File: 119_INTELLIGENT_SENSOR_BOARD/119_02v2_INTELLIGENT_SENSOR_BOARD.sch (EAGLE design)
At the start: 14 parts

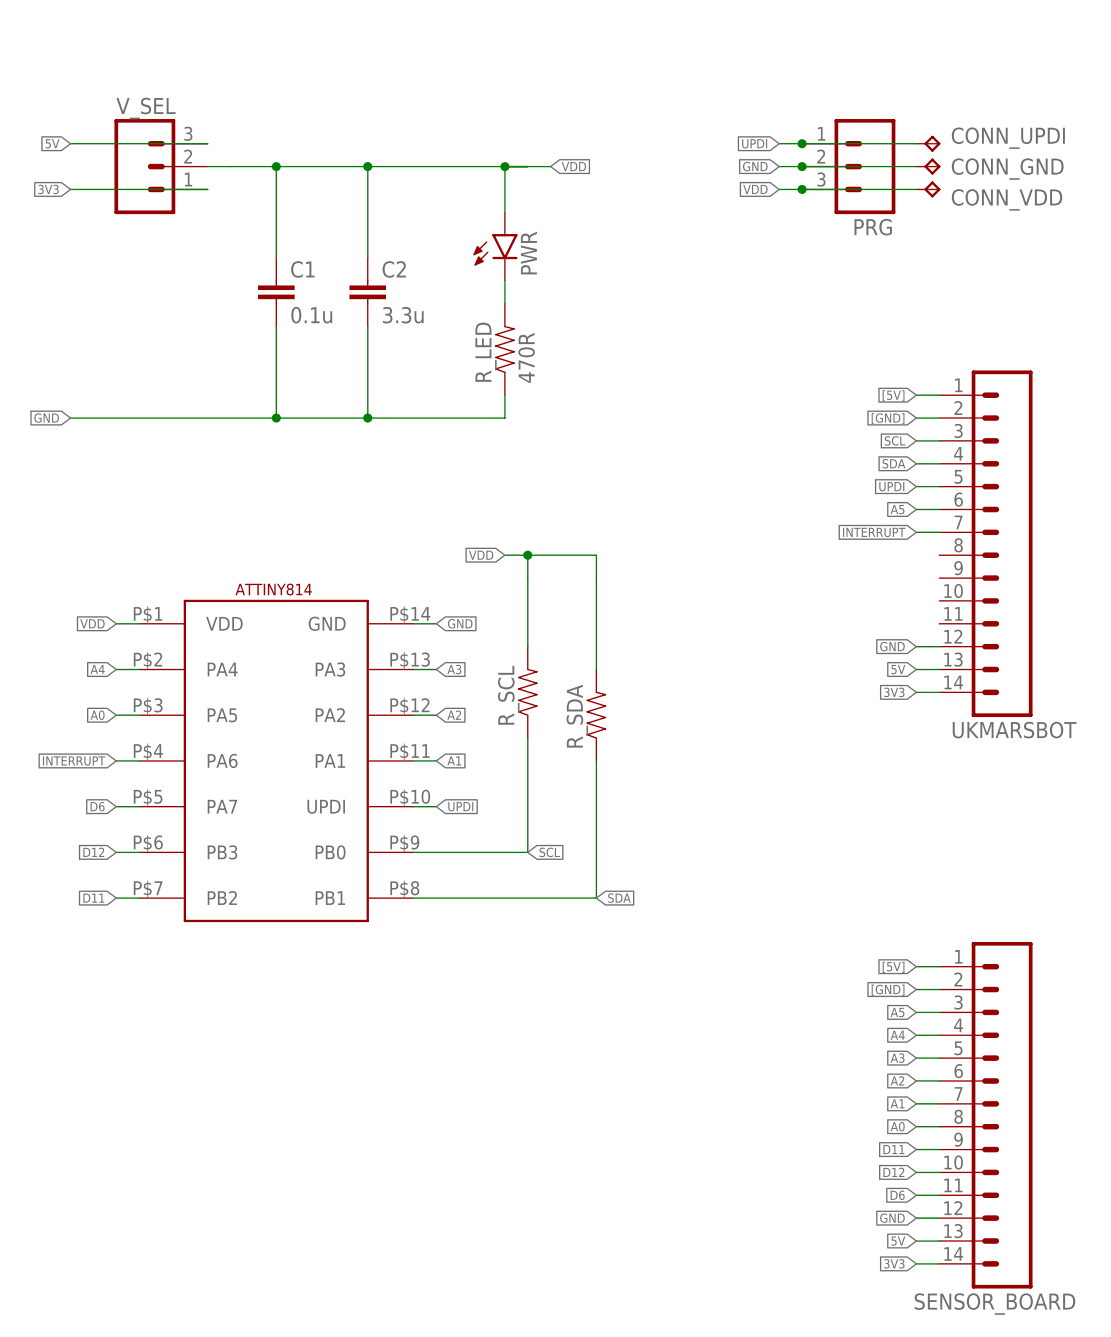
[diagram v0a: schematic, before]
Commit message: Formed new documentation
Split manual into datasheet, library and notes... added a few more ISC library header defines
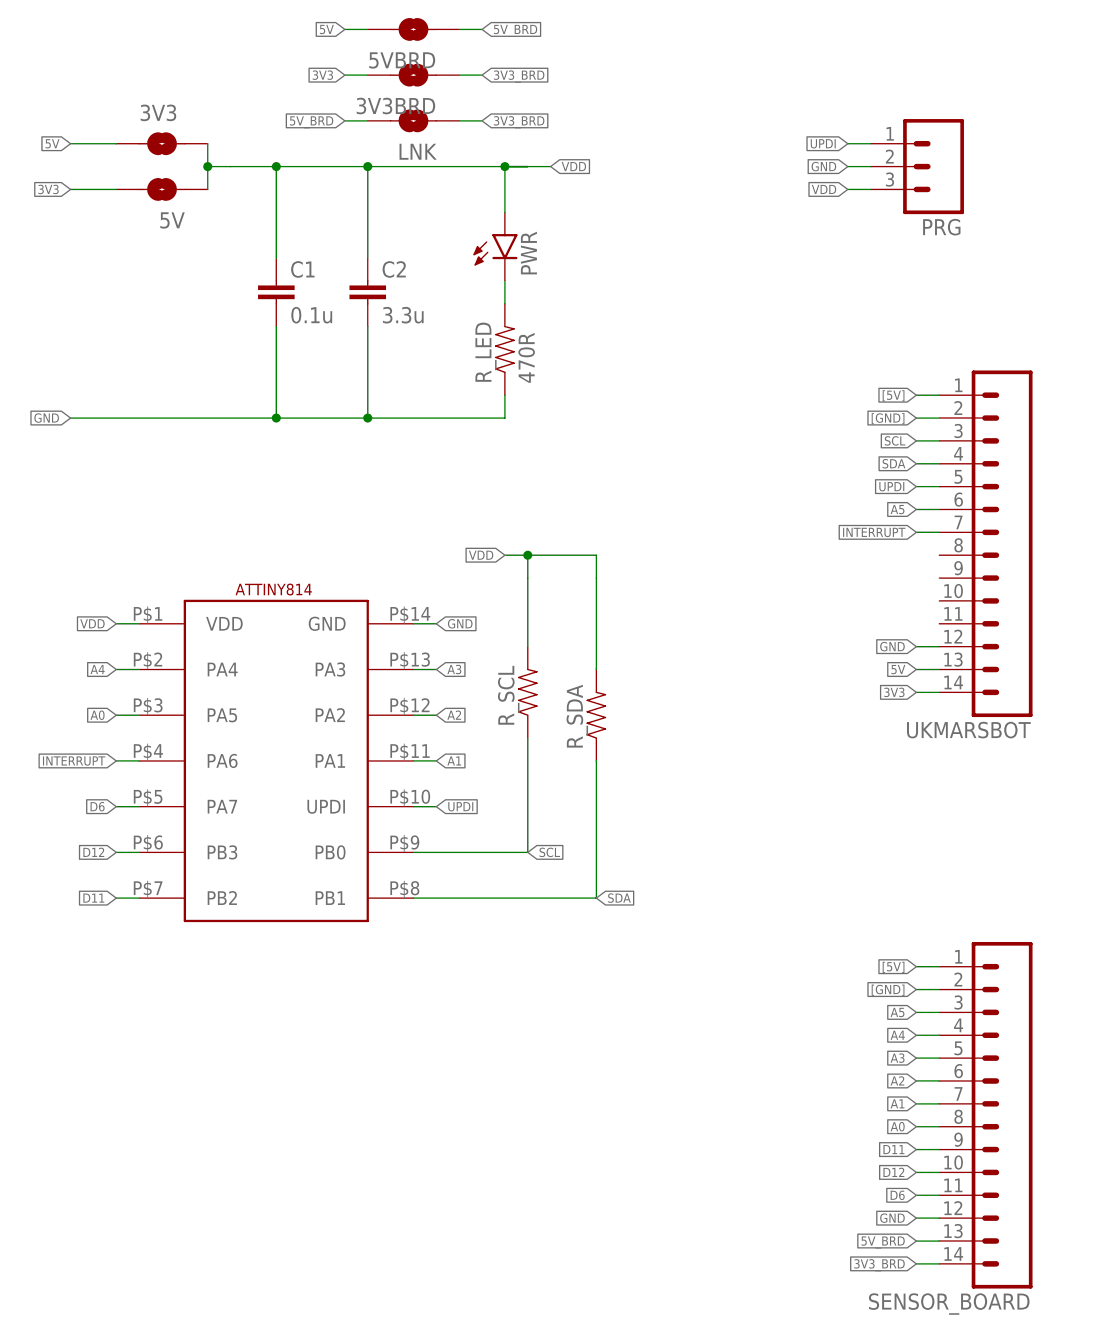
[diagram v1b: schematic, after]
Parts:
- removed CONN_GND, CONN_UPDI, CONN_VDD: TPB1,27, testpad:TPB1,27
- removed V_SEL: (no value), SparkFun-Connectors:M03PTH
- added 3V3, 3V3BRD, 5V, 5VBRD, LNK: JUMPER-SMT_2_NO_SILK, SparkFun-Jumpers:JUMPER-SMT_2_NO_SILK
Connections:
- new net 3V3_BRD: 3V3BRD.1, LNK.1, SENSOR_BOARD.14
- new net 5V_BRD: 5VBRD.1, LNK.2, SENSOR_BOARD.13
- net 3V3: now also 3V3BRD.2, 5V.2; no longer SENSOR_BOARD.14, V_SEL.1
- net 5V: now also 3V3.2, 5VBRD.2; no longer SENSOR_BOARD.13, V_SEL.3
- net GND: no longer CONN_GND.TP
- net UPDI: no longer CONN_UPDI.TP
- net VDD: now also 3V3.1, 5V.1; no longer CONN_VDD.TP, V_SEL.2
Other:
- moved on the sheet: PRG
